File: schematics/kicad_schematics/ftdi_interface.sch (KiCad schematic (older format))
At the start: 9 parts, among them U12 USB-TYPEB, U13 FT232RL

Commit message: added datasheets and modified schematic components for new dip switches
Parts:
- added C52: 1uF, SM0805, symbol C
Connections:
- wire segments 40 -> 42
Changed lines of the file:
@@
-EESchema Schematic File Version 2  date Sat 13 Mar 2010 04:13:45 PM EST
+EESchema Schematic File Version 2  date Sun 14 Mar 2010 12:34:26 PM EDT
 LIBS:power
 LIBS:device
@@
 Sheet 2 5
 Title ""
-Date "13 mar 2010"
+Date "14 mar 2010"
 Rev ""
 Comp ""
@@
 Comment4 ""
 $EndDescr
-$Comp
-L GND #PWR033
+Connection ~ 4250 3150
+Wire Wire Line
+	4250 3550 4250 3150
+Connection ~ 3050 3900
+Wire Wire Line
+	3050 4100 3050 3750
+Wire Wire Line
+	3500 2750 4350 2750
+Wire Wire Line
+	6450 4200 6900 4200
+Wire Wire Line
+	6450 3400 6800 3400
+Wire Wire Line
+	6450 3200 6800 3200
+Wire Wire Line
+	5750 2500 4600 2500
+Wire Wire Line
+	4600 2500 4600 3050
+Connection ~ 4350 3150
+Wire Wire Line
+	4350 2750 4350 3150
+Wire Wire Line
+	7700 3700 7700 3900
+Wire Wire Line
+	7700 3900 6450 3900
+Wire Wire Line
+	7700 2700 7700 2500
+Wire Wire Line
+	7700 3200 7700 3300
+Wire Wire Line
+	3050 3600 3200 3600
+Wire Wire Line
+	3200 3600 3200 3900
+Wire Wire Line
+	3200 3900 3350 3900
+Wire Wire Line
+	5550 5000 5550 5350
+Connection ~ 5550 5150
+Wire Wire Line
+	5850 5000 5850 5150
+Wire Wire Line
+	5850 5150 5250 5150
+Wire Wire Line
+	5250 5150 5250 5000
+Wire Wire Line
+	4600 3400 4600 3300
+Wire Wire Line
+	4600 3300 3050 3300
+Wire Wire Line
+	3550 3150 3050 3150
+Wire Wire Line
+	4150 3150 4600 3150
+Wire Wire Line
+	3050 3450 4500 3450
+Wire Wire Line
+	4500 3450 4500 3500
+Wire Wire Line
+	4500 3500 4600 3500
+Wire Wire Line
+	5400 5000 5400 5150
+Connection ~ 5400 5150
+Wire Wire Line
+	5700 5150 5700 5000
+Connection ~ 5700 5150
+Wire Wire Line
+	3350 3500 3350 3150
+Connection ~ 3350 3150
+Wire Wire Line
+	3350 3900 3350 4100
+Wire Wire Line
+	4450 4700 4450 4850
+Wire Wire Line
+	8000 3200 8000 3300
+Wire Wire Line
+	8000 2700 8000 2500
+Wire Wire Line
+	8000 3700 8000 4000
+Wire Wire Line
+	8000 4000 6450 4000
+Wire Wire Line
+	3750 4300 4600 4300
+Connection ~ 4450 4300
+Wire Wire Line
+	6450 3100 6800 3100
+Wire Wire Line
+	6450 3300 6800 3300
+Wire Wire Line
+	6450 4100 6900 4100
+Wire Wire Line
+	6450 4300 6900 4300
+Wire Wire Line
+	4250 3950 4250 4000
+$Comp
+L GND #PWR031
+U 1 1 4B9D0E98
+P 4250 4000
+F 0 "#PWR031" H 4250 4000 30  0001 C CNN
+F 1 "GND" H 4250 3930 30  0001 C CNN
+	1    4250 4000
+	1    0    0    -1
+$EndComp
+$Comp
+L C C52
+U 1 1 4B9D0E99
+P 4250 3750
+F 0 "C52" H 4300 3850 50  0000 L CNN
+F 1 "1uF" H 4300 3650 50  0000 L CNN
+F 2 "SM0805" H 4250 3750 60  0001 C CNN
+	1    4250 3750
+	1    0    0    -1
+$EndComp
+$Comp
+L GND #PWR032
 U 1 1 4B9840B6
 P 3050 4100
-F 0 "#PWR033" H 3050 4100 30  0001 C CNN
+F 0 "#PWR032" H 3050 4100 30  0001 C CNN
 F 1 "GND" H 3050 4030 30  0001 C CNN
 	1    3050 4100
 	1    0    0    -1
 $EndComp
-Connection ~ 3050 3900
-Wire Wire Line
-	3050 4100 3050 3750
-Wire Wire Line
-	3500 2750 4350 2750
-Wire Wire Line
-	6450 4200 6900 4200
-Wire Wire Line
-	6450 3400 6800 3400
-Wire Wire Line
-	6450 3200 6800 3200
-Wire Wire Line
-	5750 2500 4600 2500
-Wire Wire Line
-	4600 2500 4600 3050
-Connection ~ 4350 3150
-Wire Wire Line
-	4350 2750 4350 3150
-Wire Wire Line
-	7700 3700 7700 3900
-Wire Wire Line
-	7700 3900 6450 3900
-Wire Wire Line
-	7700 2700 7700 2500
-Wire Wire Line
-	7700 3200 7700 3300
-Wire Wire Line
-	3050 3600 3200 3600
-Wire Wire Line
-	3200 3600 3200 3900
-Wire Wire Line
-	3200 3900 3350 3900
-Wire Wire Line
-	5550 5000 5550 5350
-Connection ~ 5550 5150
-Wire Wire Line
-	5850 5000 5850 5150
-Wire Wire Line
-	5850 5150 5250 5150
-Wire Wire Line
-	5250 5150 5250 5000
-Wire Wire Line
-	4600 3400 4600 3300
-Wire Wire Line
-	4600 3300 3050 3300
-Wire Wire Line
-	3550 3150 3050 3150
-Wire Wire Line
-	4150 3150 4600 3150
-Wire Wire Line
-	3050 3450 4500 3450
-Wire Wire Line
-	4500 3450 4500 3500
-Wire Wire Line
-	4500 3500 4600 3500
-Wire Wire Line
-	5400 5000 5400 5150
-Connection ~ 5400 5150
-Wire Wire Line
-	5700 5150 5700 5000
-Connection ~ 5700 5150
-Wire Wire Line
-	3350 3500 3350 3150
-Connection ~ 3350 3150
-Wire Wire Line
-	3350 3900 3350 4100
-Wire Wire Line
-	4450 4700 4450 4850
-Wire Wire Line
-	8000 3200 8000 3300
-Wire Wire Line
-	8000 2700 8000 2500
-Wire Wire Line
-	8000 3700 8000 4000
-Wire Wire Line
-	8000 4000 6450 4000
-Wire Wire Line
-	3750 4300 4600 4300
-Connection ~ 4450 4300
-Wire Wire Line
-	6450 3100 6800 3100
-Wire Wire Line
-	6450 3300 6800 3300
-Wire Wire Line
-	6450 4100 6900 4100
-Wire Wire Line
-	6450 4300 6900 4300
 Text GLabel 3500 2750 0    60   Output ~ 0
 USBFTDI5V
@@
 $EndComp
 $Comp
-L GND #PWR034
+L GND #PWR033
 U 1 1 4B91C5D0
 P 4450 4850
-F 0 "#PWR034" H 4450 4850 30  0001 C CNN
+F 0 "#PWR033" H 4450 4850 30  0001 C CNN
 F 1 "GND" H 4450 4780 30  0001 C CNN
 	1    4450 4850
@@
 $EndComp
 $Comp
-L GND #PWR035
+L GND #PWR034
 U 1 1 4B91C584
 P 3350 4100
-F 0 "#PWR035" H 3350 4100 30  0001 C CNN
+F 0 "#PWR034" H 3350 4100 30  0001 C CNN
 F 1 "GND" H 3350 4030 30  0001 C CNN
 	1    3350 4100
@@
 $EndComp
 $Comp
-L GND #PWR036
+L GND #PWR035
 U 1 1 4B91C510
 P 5550 5350
-F 0 "#PWR036" H 5550 5350 30  0001 C CNN
+F 0 "#PWR035" H 5550 5350 30  0001 C CNN
 F 1 "GND" H 5550 5280 30  0001 C CNN
 	1    5550 5350

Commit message: made some usb changes
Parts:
- removed U12: USB-TYPEB, mini-usb-b, symbol USB-TYPEB
- added U12: USB-MINI-B, symbol USB-MINI-B
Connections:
- wire segments 42 -> 49
- no-connect marks 9 -> 10
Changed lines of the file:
@@
-EESchema Schematic File Version 2  date Sun 14 Mar 2010 02:53:54 PM EDT
+EESchema Schematic File Version 2  date Sun 14 Mar 2010 03:28:34 PM EDT
 LIBS:power
 LIBS:device
@@
 Comment4 ""
 $EndDescr
+NoConn ~ 3050 3600
+$Comp
+L USB-MINI-B U12
+U 1 1 4B9D38B8
+P 2650 3450
+F 0 "U12" H 2600 3900 60  0000 C CNN
+F 1 "USB-MINI-B" H 2800 3000 60  0000 C CNN
+	1    2650 3450
+	-1   0    0    -1
+$EndComp
 Connection ~ 4250 3150
 Wire Wire Line
 	4250 3550 4250 3150
-Connection ~ 3050 3900
-Wire Wire Line
-	3050 4100 3050 3750
 Wire Wire Line
 	3500 2750 4350 2750
@@
 	7700 3200 7700 3300
 Wire Wire Line
-	3050 3600 3200 3600
-Wire Wire Line
-	3200 3600 3200 3900
+	3050 3750 3200 3750
+Wire Wire Line
+	3200 3750 3200 3900
 Wire Wire Line
 	3200 3900 3350 3900
 Wire Wire Line
-	5550 5000 5550 5350
+	5550 5000 5550 5150
+Wire Wire Line
+	5550 5150 5550 5350
 Connection ~ 5550 5150
 Wire Wire Line
 	5850 5000 5850 5150
 Wire Wire Line
-	5850 5150 5250 5150
+	5850 5150 5700 5150
+Wire Wire Line
+	5700 5150 5550 5150
+Wire Wire Line
+	5550 5150 5400 5150
+Wire Wire Line
+	5400 5150 5250 5150
 Wire Wire Line
 	5250 5150 5250 5000
@@
 	4600 3300 3050 3300
 Wire Wire Line
-	3550 3150 3050 3150
-Wire Wire Line
-	4150 3150 4600 3150
+	3550 3150 3350 3150
+Wire Wire Line
+	3350 3150 3050 3150
+Wire Wire Line
+	4150 3150 4250 3150
+Wire Wire Line
+	4250 3150 4350 3150
+Wire Wire Line
+	4350 3150 4600 3150
 Wire Wire Line
 	3050 3450 4500 3450
@@
 	8000 4000 6450 4000
 Wire Wire Line
-	3750 4300 4600 4300
+	3750 4300 4450 4300
+Wire Wire Line
+	4450 4300 4600 4300
 Connection ~ 4450 4300
 Wire Wire Line
@@
 F 2 "SM0805" H 4250 3750 60  0001 C CNN
 	1    4250 3750
-	1    0    0    -1
-$EndComp
-$Comp
-L GND #PWR034
-U 1 1 4B9840B6
-P 3050 4100
-F 0 "#PWR034" H 3050 4100 30  0001 C CNN
-F 1 "GND" H 3050 4030 30  0001 C CNN
-	1    3050 4100
 	1    0    0    -1
 $EndComp
@@
 $EndComp
 $Comp
-L USB-TYPEB U12
-U 1 1 4B91C490
-P 2650 3450
-F 0 "U12" H 2600 3900 60  0000 C CNN
-F 1 "USB-TYPEB" H 2850 2850 60  0000 C CNN
-F 2 "mini-usb-b" H 2650 3450 60  0001 C CNN
-	1    2650 3450
-	-1   0    0    -1
-$EndComp
-$Comp

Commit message: modified pinout on em406, update schematic, and modified pinout on S08 and SSOT6
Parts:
- U12: footprint (none) -> mini-usb-b
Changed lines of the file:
@@
-EESchema Schematic File Version 2  date Sun 14 Mar 2010 03:28:34 PM EDT
+EESchema Schematic File Version 2  date Sun 14 Mar 2010 03:55:01 PM EDT
 LIBS:power
 LIBS:device
@@
 F 0 "U12" H 2600 3900 60  0000 C CNN
 F 1 "USB-MINI-B" H 2800 3000 60  0000 C CNN
+F 2 "mini-usb-b" H 2650 3450 60  0001 C CNN
 	1    2650 3450
 	-1   0    0    -1
@@
 	3200 3900 3350 3900
 Wire Wire Line
-	5550 5000 5550 5150
-Wire Wire Line
-	5550 5150 5550 5350
+	5550 5000 5550 5350
 Connection ~ 5550 5150
 Wire Wire Line
 	5850 5000 5850 5150
 Wire Wire Line
-	5850 5150 5700 5150
-Wire Wire Line
-	5700 5150 5550 5150
-Wire Wire Line
-	5550 5150 5400 5150
-Wire Wire Line
-	5400 5150 5250 5150
+	5850 5150 5250 5150
 Wire Wire Line
 	5250 5150 5250 5000
@@
 	4600 3300 3050 3300
 Wire Wire Line
-	3550 3150 3350 3150
-Wire Wire Line
-	3350 3150 3050 3150
-Wire Wire Line
-	4150 3150 4250 3150
-Wire Wire Line
-	4250 3150 4350 3150
-Wire Wire Line
-	4350 3150 4600 3150
+	3550 3150 3050 3150
+Wire Wire Line
+	4150 3150 4600 3150
 Wire Wire Line
 	3050 3450 4500 3450
@@
 	8000 4000 6450 4000
 Wire Wire Line
-	3750 4300 4450 4300
-Wire Wire Line
-	4450 4300 4600 4300
+	3750 4300 4600 4300
 Connection ~ 4450 4300
 Wire Wire Line
@@
 $EndComp
 $Comp
-L GND #PWR035
+L GND #PWR034
 U 1 1 4B91C5D0
 P 4450 4850
-F 0 "#PWR035" H 4450 4850 30  0001 C CNN
+F 0 "#PWR034" H 4450 4850 30  0001 C CNN
 F 1 "GND" H 4450 4780 30  0001 C CNN
 	1    4450 4850
@@
 $EndComp
 $Comp
-L GND #PWR036
+L GND #PWR035
 U 1 1 4B91C584
 P 3350 4100
-F 0 "#PWR036" H 3350 4100 30  0001 C CNN
+F 0 "#PWR035" H 3350 4100 30  0001 C CNN
 F 1 "GND" H 3350 4030 30  0001 C CNN
 	1    3350 4100
@@
 $EndComp
 $Comp
-L GND #PWR037
+L GND #PWR036
 U 1 1 4B91C510
 P 5550 5350
-F 0 "#PWR037" H 5550 5350 30  0001 C CNN
+F 0 "#PWR036" H 5550 5350 30  0001 C CNN
 F 1 "GND" H 5550 5280 30  0001 C CNN
 	1    5550 5350

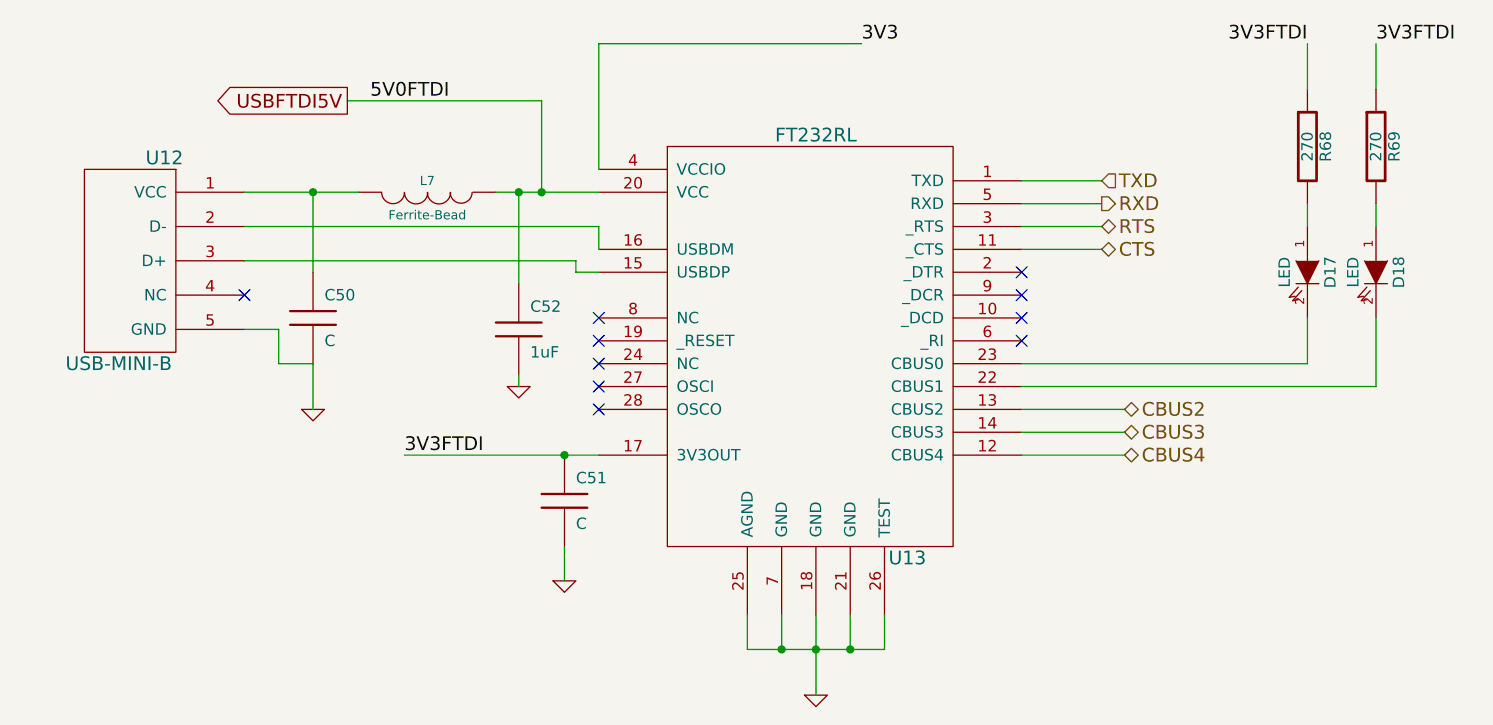
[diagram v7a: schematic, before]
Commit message: Modified power libraries. Now using custom power.lib. This is important Removed outdated crystal libaries Changed some caps to 0603 mounts started PCB layout
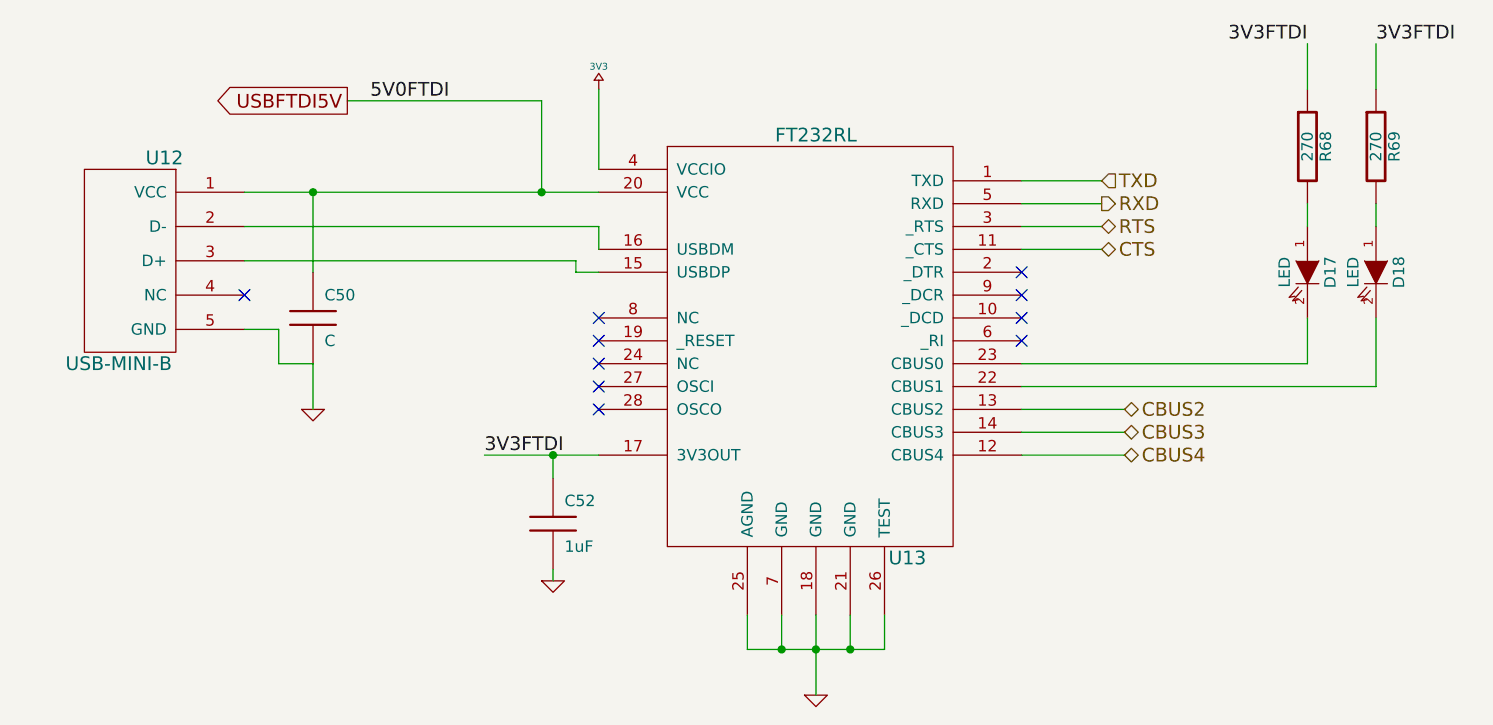
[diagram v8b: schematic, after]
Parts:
- removed C51: C, SM0805, symbol C
- removed L7: Ferrite-Bead, SM0805, symbol INDUCTOR
- C50, C52, R68, R69: footprint SM0805 -> SM0805-CUSTOM
- D17, D18: footprint LED-0805 -> LED-0805-CUS
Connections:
- net 3V3FTDI: now also C52.1
- net USBFTDI5V: now also C50.1, U12.1 (VCC); no longer C52.1
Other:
- moved on the sheet: C52
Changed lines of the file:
@@
-EESchema Schematic File Version 2  date Mon 15 Mar 2010 09:49:52 PM EDT
+EESchema Schematic File Version 2  date Tue 16 Mar 2010 05:07:11 PM EDT
 LIBS:power
 LIBS:device
@@
 Comment4 ""
 $EndDescr
+$Comp
+L GND #PWR035
+U 1 1 4B9FD9E1
+P 3350 4100
+F 0 "#PWR035" H 3350 4100 30  0001 C CNN
+F 1 "GND" H 3350 4030 30  0001 C CNN
+	1    3350 4100
+	1    0    0    -1
+$EndComp
+Connection ~ 4400 4300
+Wire Wire Line
+	4400 4400 4400 4300
+Wire Wire Line
+	3500 2750 4350 2750
+Wire Wire Line
+	6450 4200 6900 4200
+Wire Wire Line
+	6450 3400 6800 3400
+Wire Wire Line
+	6450 3200 6800 3200
+Wire Wire Line
+	4600 3050 4600 2700
+Connection ~ 4350 3150
+Wire Wire Line
+	4350 2750 4350 3150
+Wire Wire Line
+	7700 3700 7700 3900
+Wire Wire Line
+	7700 3900 6450 3900
+Wire Wire Line
+	7700 2700 7700 2500
+Wire Wire Line
+	7700 3200 7700 3300
+Wire Wire Line
+	3050 3750 3200 3750
+Wire Wire Line
+	3200 3750 3200 3900
+Wire Wire Line
+	3200 3900 3350 3900
+Wire Wire Line
+	5550 5350 5550 5000
+Connection ~ 5550 5150
+Wire Wire Line
+	5850 5000 5850 5150
+Wire Wire Line
+	5850 5150 5250 5150
+Wire Wire Line
+	5250 5150 5250 5000
+Wire Wire Line
+	4600 3400 4600 3300
+Wire Wire Line
+	4600 3300 3050 3300
+Wire Wire Line
+	3050 3150 4600 3150
+Wire Wire Line
+	3050 3450 4500 3450
+Wire Wire Line
+	4500 3450 4500 3500
+Wire Wire Line
+	4500 3500 4600 3500
+Wire Wire Line
+	5400 5000 5400 5150
+Connection ~ 5400 5150
+Wire Wire Line
+	5700 5150 5700 5000
+Connection ~ 5700 5150
+Wire Wire Line
+	3350 3500 3350 3150
+Connection ~ 3350 3150
+Wire Wire Line
+	3350 3900 3350 4100
+Wire Wire Line
+	8000 3200 8000 3300
+Wire Wire Line
+	8000 2700 8000 2500
+Wire Wire Line
+	8000 3700 8000 4000
+Wire Wire Line
+	8000 4000 6450 4000
+Wire Wire Line
+	6450 3100 6800 3100
+Wire Wire Line
+	6450 3300 6800 3300
+Wire Wire Line
+	6450 4100 6900 4100
+Wire Wire Line
+	6450 4300 6900 4300
+Wire Wire Line
+	4400 4800 4400 4850
+Wire Wire Line
+	4600 4300 4100 4300
+$Comp
+L GND #PWR036
+U 1 1 4B9FD9B6
+P 5550 5350
+F 0 "#PWR036" H 5550 5350 30  0001 C CNN
+F 1 "GND" H 5550 5280 30  0001 C CNN
+	1    5550 5350
+	1    0    0    -1
+$EndComp
+$Comp
+L 3V3 #PWR037
+U 1 1 4B9FD9B2
+P 4600 2700
+F 0 "#PWR037" H 4600 2830 20  0001 C CNN
+F 1 "3V3" H 4600 2800 30  0000 C CNN
+	1    4600 2700
+	1    0    0    -1
+$EndComp
+$Comp
+L GND #PWR038
+U 1 1 4B9FD9AD
+P 4400 4850
+F 0 "#PWR038" H 4400 4850 30  0001 C CNN
+F 1 "GND" H 4400 4780 30  0001 C CNN
+	1    4400 4850
+	1    0    0    -1
+$EndComp
+$Comp
+L C C52
+U 1 1 4B9D0E99
+P 4400 4600
+F 0 "C52" H 4450 4700 50  0000 L CNN
+F 1 "1uF" H 4450 4500 50  0000 L CNN
+F 2 "SM0805-CUSTOM" H 4400 4600 60  0001 C CNN
+	1    4400 4600
+	1    0    0    -1
+$EndComp
+Text Label 4100 4300 0    60   ~ 0
+3V3FTDI
 NoConn ~ 3050 3600
 $Comp
@@
 	-1   0    0    -1
 $EndComp
-Connection ~ 4250 3150
-Wire Wire Line
-	4250 3550 4250 3150
-Wire Wire Line
-	3500 2750 4350 2750
-Wire Wire Line
-	6450 4200 6900 4200
-Wire Wire Line
-	6450 3400 6800 3400
-Wire Wire Line
-	6450 3200 6800 3200
-Wire Wire Line
-	5750 2500 4600 2500
-Wire Wire Line
-	4600 2500 4600 3050
-Connection ~ 4350 3150
-Wire Wire Line
-	4350 2750 4350 3150
-Wire Wire Line
-	7700 3700 7700 3900
-Wire Wire Line
-	7700 3900 6450 3900
-Wire Wire Line
-	7700 2700 7700 2500
-Wire Wire Line
-	7700 3200 7700 3300
-Wire Wire Line
-	3050 3750 3200 3750
-Wire Wire Line
-	3200 3750 3200 3900
-Wire Wire Line
-	3200 3900 3350 3900
-Wire Wire Line
-	5550 5000 5550 5350
-Connection ~ 5550 5150
-Wire Wire Line
-	5850 5000 5850 5150
-Wire Wire Line
-	5850 5150 5250 5150
-Wire Wire Line
-	5250 5150 5250 5000
-Wire Wire Line
-	4600 3400 4600 3300
-Wire Wire Line
-	4600 3300 3050 3300
-Wire Wire Line
-	3550 3150 3050 3150
-Wire Wire Line
-	4150 3150 4600 3150
-Wire Wire Line
-	3050 3450 4500 3450
-Wire Wire Line
-	4500 3450 4500 3500
-Wire Wire Line
-	4500 3500 4600 3500
-Wire Wire Line
-	5400 5000 5400 5150
-Connection ~ 5400 5150
-Wire Wire Line
-	5700 5150 5700 5000
-Connection ~ 5700 5150
-Wire Wire Line
-	3350 3500 3350 3150
-Connection ~ 3350 3150
-Wire Wire Line
-	3350 3900 3350 4100
-Wire Wire Line
-	4450 4700 4450 4850
-Wire Wire Line
-	8000 3200 8000 3300
-Wire Wire Line
-	8000 2700 8000 2500
-Wire Wire Line
-	8000 3700 8000 4000
-Wire Wire Line
-	8000 4000 6450 4000
-Wire Wire Line
-	3750 4300 4600 4300
-Connection ~ 4450 4300
-Wire Wire Line
-	6450 3100 6800 3100
-Wire Wire Line
-	6450 3300 6800 3300
-Wire Wire Line
-	6450 4100 6900 4100
-Wire Wire Line
-	6450 4300 6900 4300
-Wire Wire Line
-	4250 3950 4250 4000
-$Comp
-L GND #PWR75
-U 1 1 4B9D0E98
-P 4250 4000
-F 0 "#PWR75" H 4250 4000 30  0001 C CNN
-F 1 "GND" H 4250 3930 30  0001 C CNN
-	1    4250 4000
-	1    0    0    -1
-$EndComp
-$Comp
-L C C52
-U 1 1 4B9D0E99
-P 4250 3750
-F 0 "C52" H 4300 3850 50  0000 L CNN
-F 1 "1uF" H 4300 3650 50  0000 L CNN
-F 2 "SM0805" H 4250 3750 60  0001 C CNN
-	1    4250 3750
-	1    0    0    -1
-$EndComp
 Text GLabel 3500 2750 0    60   Output ~ 0
 USBFTDI5V
@@
 Text HLabel 6900 4100 2    60   BiDi ~ 0
 CBUS2
-Text Label 5750 2500 0    60   ~ 0
-3V3
 Text HLabel 6800 3400 2    60   BiDi ~ 0
 CTS
@@
 Text Label 8000 2500 0    60   ~ 0
 3V3FTDI
-Text Label 3750 4300 0    60   ~ 0
-3V3FTDI
 NoConn ~ 4600 4100
 NoConn ~ 4600 4000
@@
 F 0 "R69" V 8080 2950 50  0000 C CNN
 F 1 "270" V 8000 2950 50  0000 C CNN
-F 2 "SM0805" H 8000 2950 60  0001 C CNN
+F 2 "SM0805-CUSTOM" H 8000 2950 60  0001 C CNN
 	1    8000 2950
 	1    0    0    -1
@@
 F 0 "R68" V 7780 2950 50  0000 C CNN
 F 1 "270" V 7700 2950 50  0000 C CNN
-F 2 "SM0805" H 7700 2950 60  0001 C CNN
+F 2 "SM0805-CUSTOM" H 7700 2950 60  0001 C CNN
 	1    7700 2950
 	1    0    0    -1
@@
 F 0 "D18" H 8000 3600 50  0000 C CNN
 F 1 "LED" H 8000 3400 50  0000 C CNN
-F 2 "LED-0805" H 8000 3500 60  0001 C CNN
+F 2 "LED-0805-CUS" H 8000 3500 60  0001 C CNN
 	1    8000 3500
 	0    1    1    0
@@
 F 0 "D17" H 7700 3600 50  0000 C CNN
 F 1 "LED" H 7700 3400 50  0000 C CNN
-F 2 "LED-0805" H 7700 3500 60  0001 C CNN
+F 2 "LED-0805-CUS" H 7700 3500 60  0001 C CNN
 	1    7700 3500
 	0    1    1    0
-$EndComp
-$Comp
-L GND #PWR76
-U 1 1 4B91C5D0
-P 4450 4850
-F 0 "#PWR76" H 4450 4850 30  0001 C CNN
-F 1 "GND" H 4450 4780 30  0001 C CNN
-	1    4450 4850
-	1    0    0    -1
-$EndComp
-$Comp
-L C C51
-U 1 1 4B91C5C7
-P 4450 4500
-F 0 "C51" H 4500 4600 50  0000 L CNN
-F 1 "C" H 4500 4400 50  0000 L CNN
-F 2 "SM0805" H 4450 4500 60  0001 C CNN
-	1    4450 4500
-	1    0    0    -1
-$EndComp
-$Comp
-L GND #PWR74
-U 1 1 4B91C584
-P 3350 4100
-F 0 "#PWR74" H 3350 4100 30  0001 C CNN
-F 1 "GND" H 3350 4030 30  0001 C CNN
-	1    3350 4100
-	1    0    0    -1
 $EndComp
 $Comp
@@
 F 0 "C50" H 3400 3800 50  0000 L CNN
 F 1 "C" H 3400 3600 50  0000 L CNN
-F 2 "SM0805" H 3350 3700 60  0001 C CNN
+F 2 "SM0805-CUSTOM" H 3350 3700 60  0001 C CNN
 	1    3350 3700
 	1    0    0    -1
 $EndComp
 $Comp
-L GND #PWR77
-U 1 1 4B91C510
-P 5550 5350
-F 0 "#PWR77" H 5550 5350 30  0001 C CNN
-F 1 "GND" H 5550 5280 30  0001 C CNN
-	1    5550 5350
-	1    0    0    -1
-$EndComp
-$Comp
-L INDUCTOR L7
-U 1 1 4B91C4C6
-P 3850 3150
-F 0 "L7" V 3800 3150 40  0000 C CNN
-F 1 "Ferrite-Bead" V 3950 3150 40  0000 C CNN
-F 2 "SM0805" H 3850 3150 60  0001 C CNN
-	1    3850 3150
-	0    1    1    0
-$EndComp
-$Comp
